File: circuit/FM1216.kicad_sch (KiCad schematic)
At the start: 61 parts, among them J1 DE9_Pins, J2 AudioJack, Q1 BC850, SW1 RotaryEncode, SW2 REREAD, U1 PIC16F876-XXISO, U2 MAX232, U3 PCF8574T, U4 L7805, Y1 20MHz

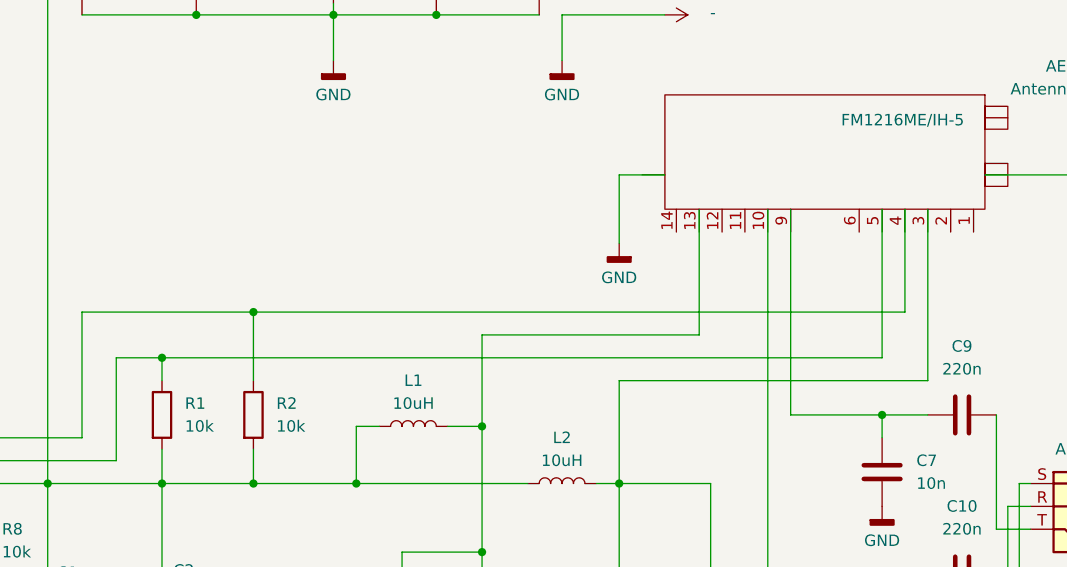
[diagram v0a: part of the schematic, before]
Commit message: Fix pin fm1216 on circuit
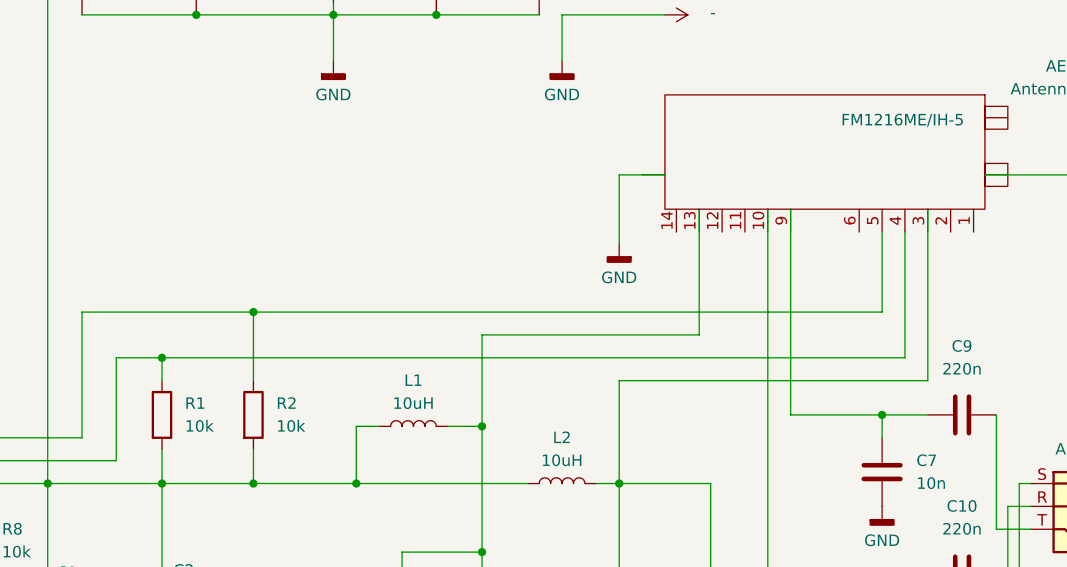
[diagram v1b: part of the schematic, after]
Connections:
- net at R1.1, R13.2, U1.14 (RC3/SCK/SCL)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: no longer FM1216ME/IH-5.5 (SDA)
- net at R16.2, R2.1, U1.15 (RC4/SDI/SDA)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: no longer FM1216ME/IH-5.4 (SCL)
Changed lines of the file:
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@@
+	(wire
+		(pts
+			(xy 255.27 53.34) (xy 255.27 62.23)
+		)
+		(stroke
+			(width 0)
+			(type default)
+		)
+	)
 	(wire
 		(pts
@@
 	(wire
 		(pts
-			(xy 257.81 62.23) (xy 185.42 62.23)
-		)
-		(stroke
-			(width 0)
-			(type default)
-		)
-	)
-	(wire
-		(pts
 			(xy 255.27 91.44) (xy 260.35 91.44)
 		)
@@
 	(wire
 		(pts
+			(xy 257.81 53.34) (xy 257.81 67.31)
+		)
+		(stroke
+			(width 0)
+			(type default)
+		)
+	)
+	(wire
+		(pts
 			(xy 162.56 100.33) (xy 162.56 101.6)
 		)
@@
 	(wire
 		(pts
-			(xy 257.81 50.8) (xy 257.81 62.23)
-		)
-		(stroke
-			(width 0)
-			(type default)
-		)
-	)
-	(wire
-		(pts
 			(xy 115.57 55.88) (xy 113.03 55.88)
 		)
@@
 	(wire
 		(pts
-			(xy 255.27 50.8) (xy 255.27 67.31)
-		)
-		(stroke
-			(width 0)
-			(type default)
-		)
-	)
-	(wire
-		(pts
 			(xy 279.4 46.99) (xy 279.4 40.64)
 		)
@@
 	(wire
 		(pts
-			(xy 175.26 67.31) (xy 255.27 67.31)
+			(xy 175.26 67.31) (xy 257.81 67.31)
 		)
 		(stroke
@@
 		)
 		(stroke
+			(width 0)
+			(type default)
+		)
+	)
+	(wire
+		(pts
+			(xy 255.27 62.23) (xy 185.42 62.23)
+		)
+		(stroke
